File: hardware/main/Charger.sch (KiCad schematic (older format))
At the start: 37 parts, among them K1 DIPxx-1Axx-13x, K2 SANYOU_SRD_Form_C, Q1 Q_NPN_BEC, Q2 BCV27, Q3 BCV27

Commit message: TO-DO List criada na folha principal
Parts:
- R13: value 450 -> 470
- gave numbers to parts that had none: 7
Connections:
- net +12V: no longer D2.1 (K), K2.5, R13.1
- new net +5V: D2.1 (K), K2.5, R13.1
- no-connect marks 0 -> 1
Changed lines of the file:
@@
 Wire Wire Line
 	2850 2100 2850 1950
-$Comp
-L power:+12V #PWR0111
-U 1 1 5C9EB031
-P 3700 4900
-F 0 "#PWR0111" H 3700 4750 50  0001 C CNN
-F 1 "+12V" H 3715 5073 50  0000 C CNN
-F 2 "" H 3700 4900 50  0001 C CNN
-F 3 "" H 3700 4900 50  0001 C CNN
-	1    3700 4900
-	1    0    0    -1
-$EndComp
-Wire Wire Line
-	3700 4900 3700 4950
 Text Label 2400 1250 2    50   ~ 0
 U_BAT+
@@
 S_RL_ON
 $Comp
-L power:+12V #PWR02
-U 1 1 5C9F0E54
-P 8100 1350
-F 0 "#PWR02" H 8100 1200 50  0001 C CNN
-F 1 "+12V" H 8115 1523 50  0000 C CNN
-F 2 "" H 8100 1350 50  0001 C CNN
-F 3 "" H 8100 1350 50  0001 C CNN
-	1    8100 1350
-	1    0    0    -1
-$EndComp
-$Comp
 L Device:R_Small_US R13
 U 1 1 5C9F0F2F
 P 8100 1650
 F 0 "R13" H 8150 1700 50  0000 L CNN
-F 1 "450" H 8168 1605 50  0000 L CNN
+F 1 "470" H 8168 1605 50  0000 L CNN
 F 2 "" H 8100 1650 50  0001 C CNN
 F 3 "~" H 8100 1650 50  0001 C CNN
@@
 VISUAL_INDICATION\n
 $Comp
-L Mechanical:MountingHole_Pad H?
+L Mechanical:MountingHole_Pad H206
 U 1 1 5CA37EF3
 P 6550 4900
-F 0 "H?" V 6504 5050 50  0000 L CNN
+F 0 "H206" V 6504 5050 50  0000 L CNN
 F 1 "U_BAT-" V 6595 5050 50  0000 L CNN
 F 2 "" H 6550 4900 50  0001 C CNN
@@
 $EndComp
 $Comp
-L Mechanical:MountingHole_Pad H?
+L Mechanical:MountingHole_Pad H207
 U 1 1 5CA39D8E
 P 8250 4900
-F 0 "H?" V 8204 5050 50  0000 L CNN
+F 0 "H207" V 8204 5050 50  0000 L CNN
 F 1 "F_BAT-" V 8295 5050 50  0000 L CNN
 F 2 "" H 8250 4900 50  0001 C CNN
@@
 MAIN FUSE
 $Comp
-L Mechanical:MountingHole_Pad H?
+L Mechanical:MountingHole_Pad H203
 U 1 1 5CA4A13E
 P 1950 1250
-F 0 "H?" V 1904 1400 50  0000 L CNN
+F 0 "H203" V 1904 1400 50  0000 L CNN
 F 1 "U_BAT+" V 1995 1400 50  0000 L CNN
 F 2 "" H 1950 1250 50  0001 C CNN
@@
 P 9500 1550
 AR Path="/5CA5F768" Ref="H?"  Part="1"
-AR Path="/5C9C4D6B/5CA5F768" Ref="H?"  Part="1"
-F 0 "H?" H 9600 1600 50  0000 L CNN
+AR Path="/5C9C4D6B/5CA5F768" Ref="H205"  Part="1"
+F 0 "H205" H 9600 1600 50  0000 L CNN
 F 1 "MountingHole" H 9600 1550 50  0000 L CNN
 F 2 "MountingHole:MountingHole_3.2mm_M3" H 9500 1550 50  0001 C CNN
@@
 P 9500 1350
 AR Path="/5CA5F76E" Ref="H?"  Part="1"
-AR Path="/5C9C4D6B/5CA5F76E" Ref="H?"  Part="1"
-F 0 "H?" H 9600 1400 50  0000 L CNN
+AR Path="/5C9C4D6B/5CA5F76E" Ref="H204"  Part="1"
+F 0 "H204" H 9600 1400 50  0000 L CNN
 F 1 "MountingHole" H 9600 1350 50  0000 L CNN
 F 2 "MountingHole:MountingHole_3.2mm_M3" H 9500 1350 50  0001 C CNN
@@
 P 9500 1150
 AR Path="/5CA5F774" Ref="H?"  Part="1"
-AR Path="/5C9C4D6B/5CA5F774" Ref="H?"  Part="1"
-F 0 "H?" H 9600 1200 50  0000 L CNN
+AR Path="/5C9C4D6B/5CA5F774" Ref="H202"  Part="1"
+F 0 "H202" H 9600 1200 50  0000 L CNN
 F 1 "MountingHole" H 9600 1150 50  0000 L CNN
 F 2 "MountingHole:MountingHole_3.2mm_M3" H 9500 1150 50  0001 C CNN
@@
 P 9500 950
 AR Path="/5CA5F77A" Ref="H?"  Part="1"
-AR Path="/5C9C4D6B/5CA5F77A" Ref="H?"  Part="1"
-F 0 "H?" H 9600 1000 50  0000 L CNN
+AR Path="/5C9C4D6B/5CA5F77A" Ref="H201"  Part="1"
+F 0 "H201" H 9600 1000 50  0000 L CNN
 F 1 "MountingHole" H 9600 950 50  0000 L CNN
 F 2 "MountingHole:MountingHole_3.2mm_M3" H 9500 950 50  0001 C CNN
@@
 U_BAT-
 $Comp
-L power:GNDPWR #PWR?
+L power:GNDPWR #PWR0101
 U 1 1 5CA63142
 P 7700 5250
-F 0 "#PWR?" H 7700 5050 50  0001 C CNN
+F 0 "#PWR0101" H 7700 5050 50  0001 C CNN
 F 1 "GNDPWR" H 7704 5096 50  0000 C CNN
 F 2 "" H 7700 5200 50  0001 C CNN
@@
 Wire Wire Line
 	7700 5200 7700 4900
+NoConn ~ 3300 4650
+$Comp
+L power:+5V #PWR?
+U 1 1 5CA9CA1B
+P 8100 1350
+F 0 "#PWR?" H 8100 1200 50  0001 C CNN
+F 1 "+5V" H 8150 1550 50  0000 C CNN
+F 2 "" H 8100 1350 50  0001 C CNN
+F 3 "" H 8100 1350 50  0001 C CNN
+	1    8100 1350
+	1    0    0    -1
+$EndComp
+Text HLabel 3700 4950 2    50   Output ~ 0
++5V
 $EndSCHEMATC

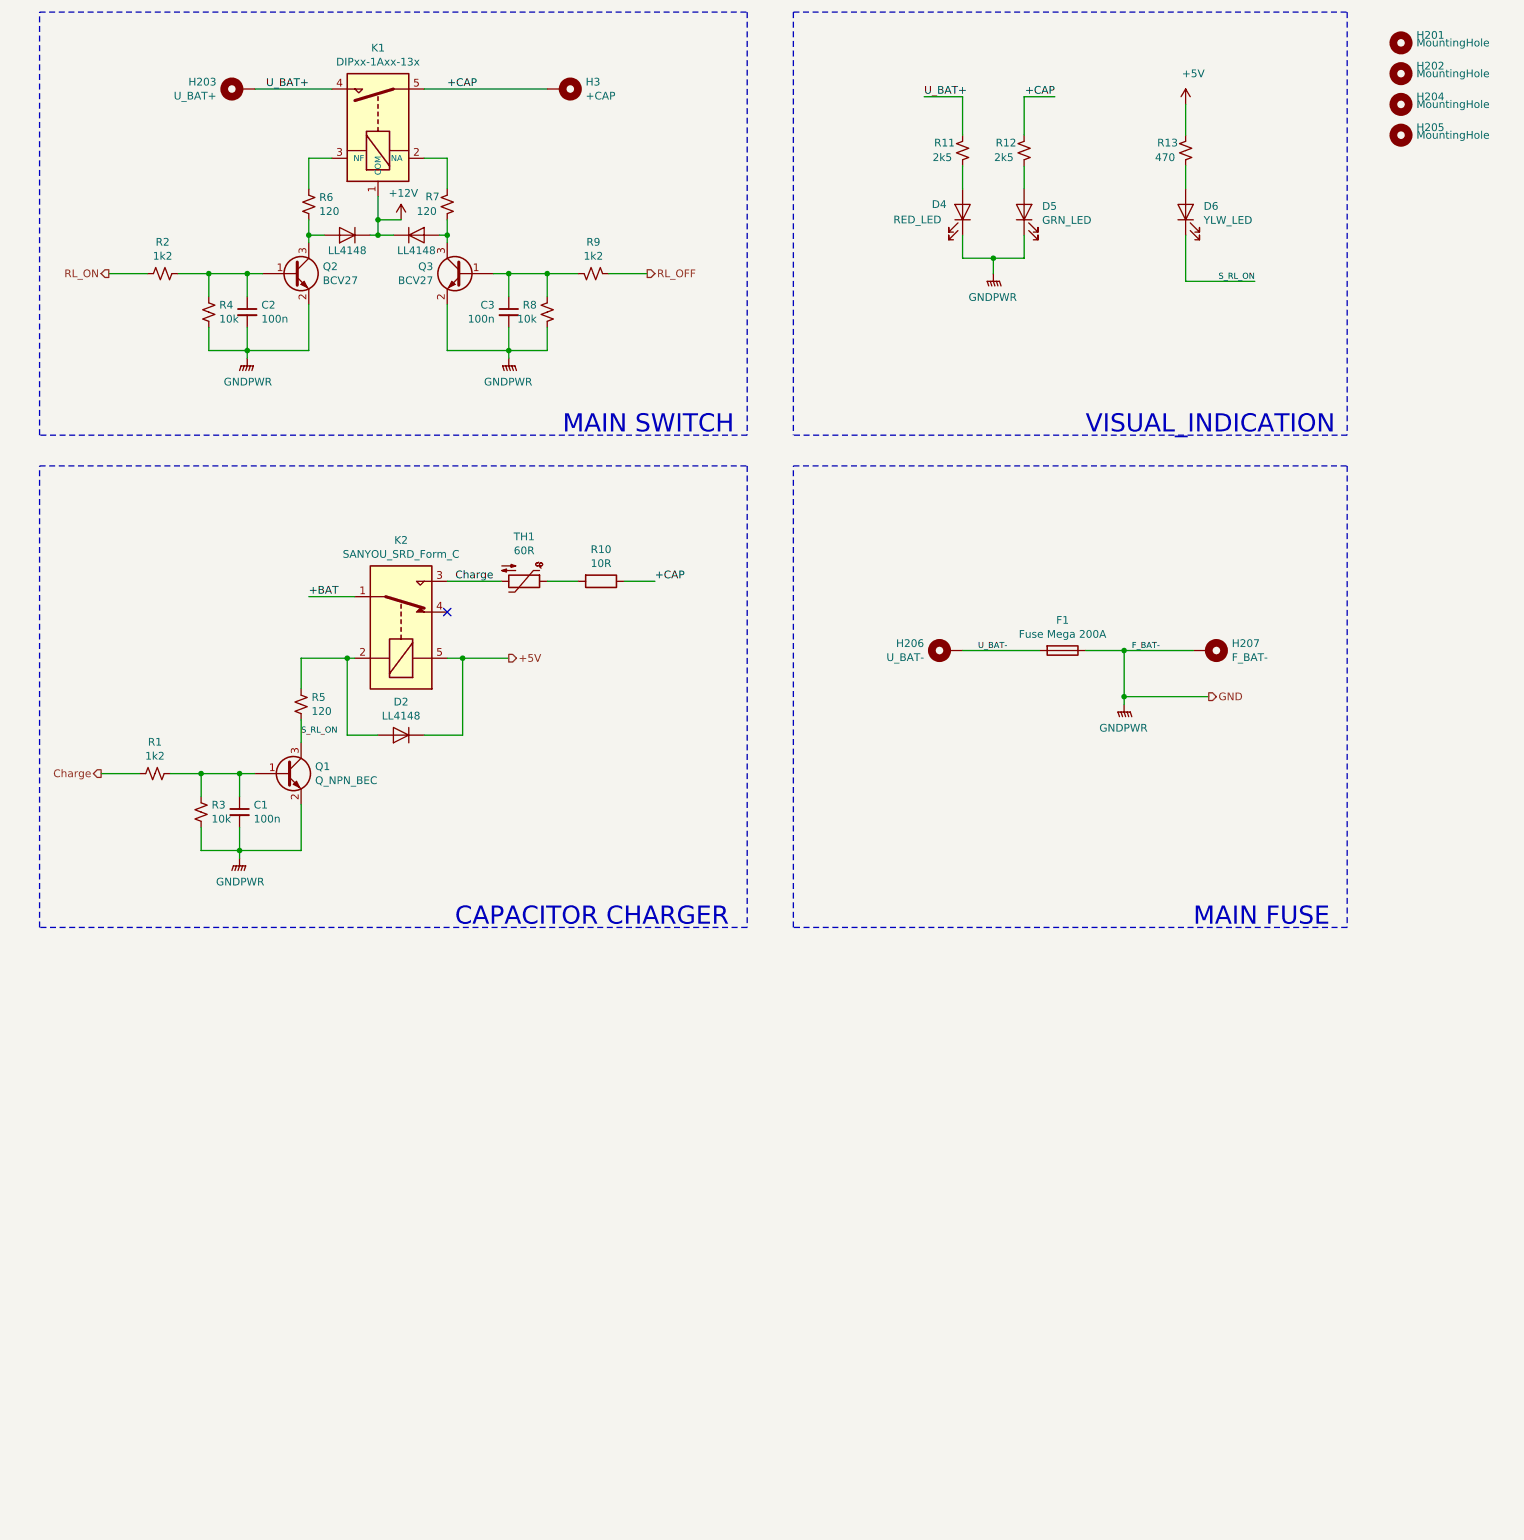
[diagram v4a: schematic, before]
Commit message: Alimentação de 12V criada no Charger, que recebe 18V do Controller
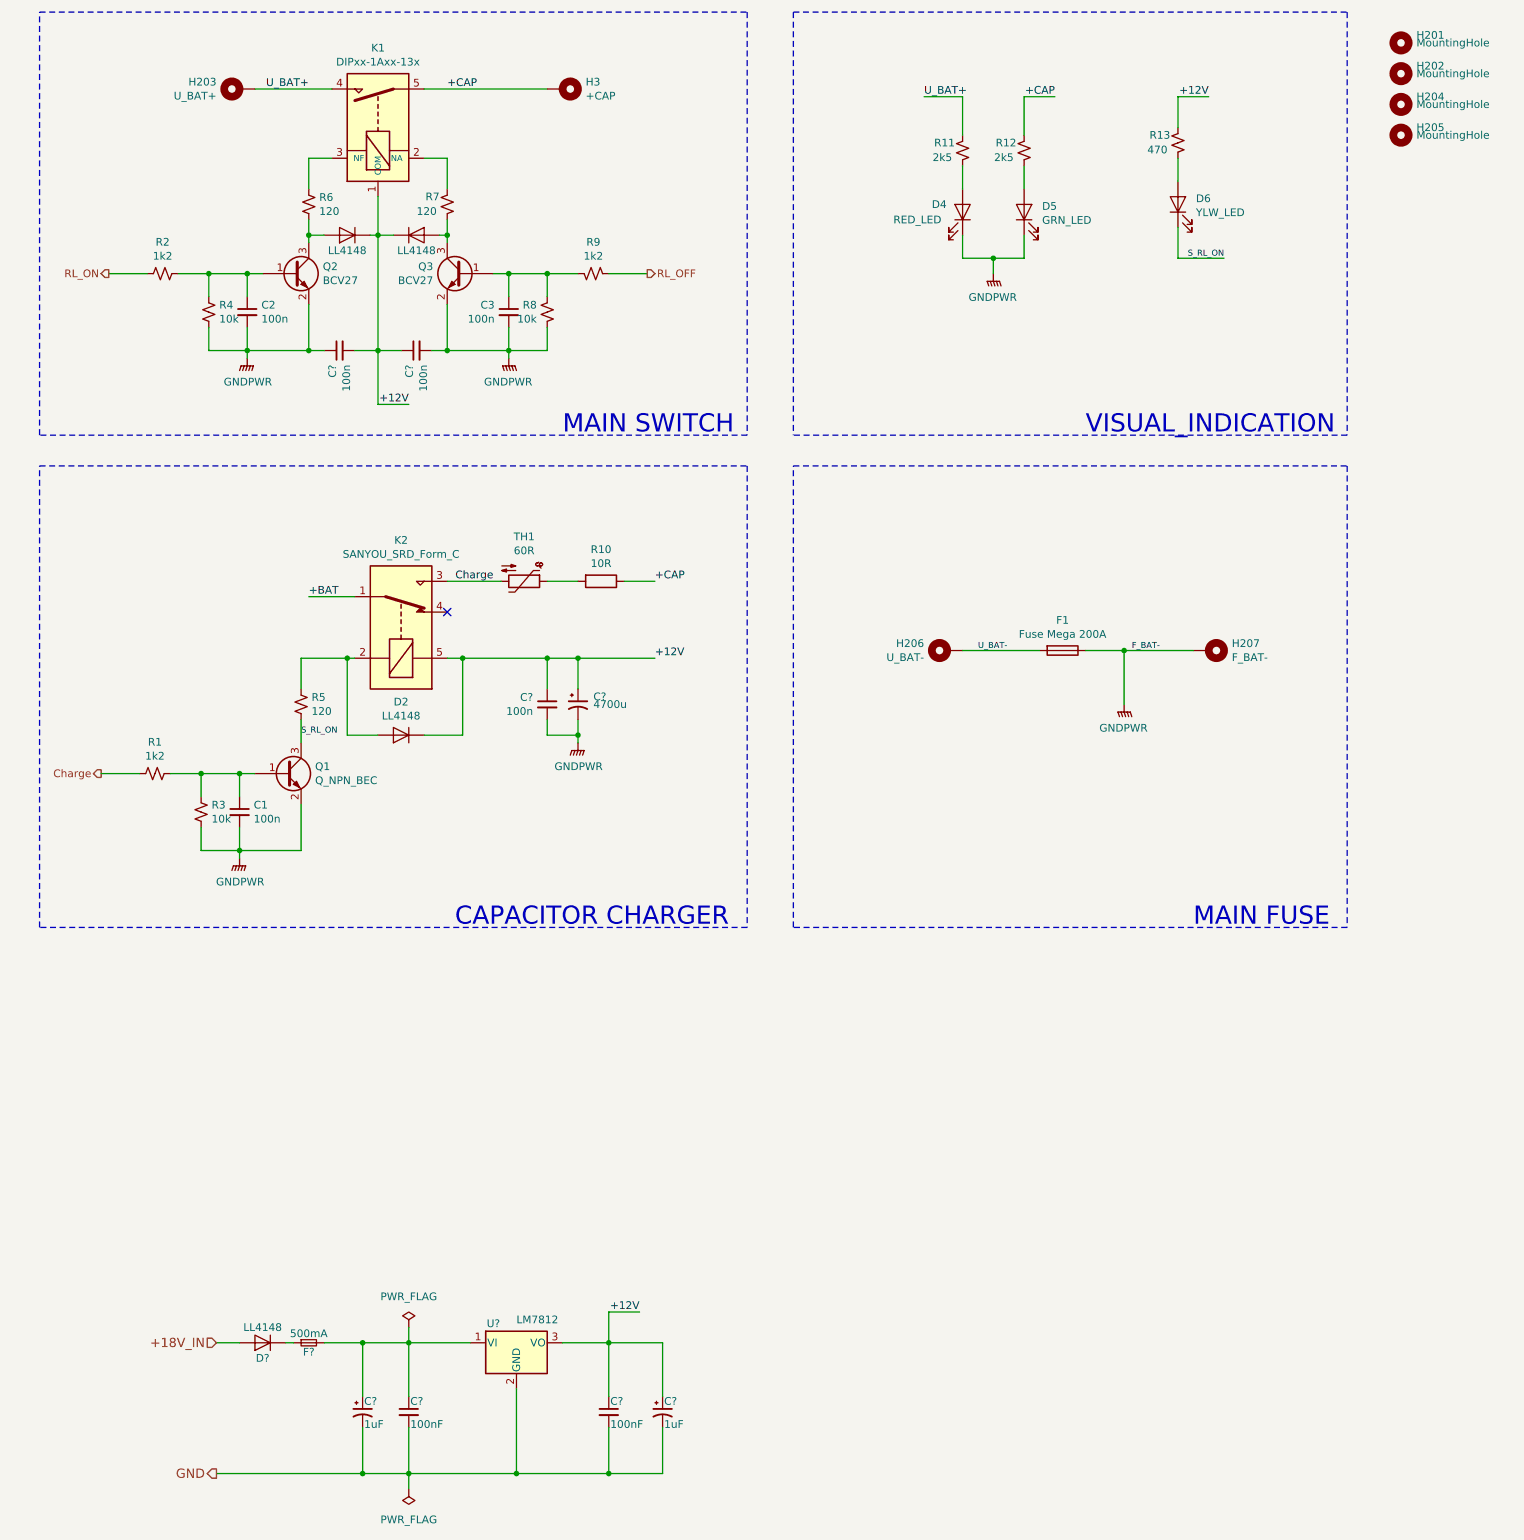
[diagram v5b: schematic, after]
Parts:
- added C?: 4700u, symbol Device:CP1_Small
- added C? (x3): 100n, symbol Device:C_Small
- added C? (x2): 1uF, Capacitor_Tantalum_SMD:CP_EIA-6032-20_AVX-F_Pad2.25x2.35mm_HandSolder, symbol Device:CP1_Small
- added C? (x2): 100nF, Capacitor_SMD:C_0805_2012Metric_Pad1.15x1.40mm_HandSolder, symbol Device:C_Small
- added D?: LL4148, Diode_SMD:D_MiniMELF_Handsoldering, symbol Diode:LL4148
- added F?: 500mA, Fuse:Fuse_1206_3216Metric_Pad1.42x1.75mm_HandSolder, symbol Device:Fuse_Small
- added U?: LM7812, KicadZeniteSolarLibrary18:TO-220-3_Horizontal_TabDown_SMD, symbol Regulator_Linear:LM7805_TO220
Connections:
- net +5V is gone; now on net +12V: D2.1 (K), K2.5, R13.1
- net +12V: now also C?.1, C?.1, C?.1, C?.1, C?.1, C?.2, U?.3 (VO)
- net GNDPWR: now also C?.1, C?.2, C?.2, C?.2
- new net: C?.1, C?.1, F?.2, U?.1 (VI)
- new net: D?.1 (K), F?.1
- new net +18V_IN: D?.2 (A)
- new net GND: C?.2, C?.2, C?.2, C?.2, U?.2 (GND)
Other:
- moved on the sheet: D6, R13
